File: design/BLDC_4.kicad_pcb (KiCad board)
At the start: 2 copper layers, 80 x 48.9 mm, 101 parts, among them J1 Conn_01x04, P1 PWR_COMM, P2 IN+, P3 IN-, P4 MOTOR3, P5 MOTOR2, P6 MOTOR1, P7 SWD, Q1 Si2302CDS, Q2 Si2302CDS, Q3 Si2302CDS, Q4 Si2302CDS, Q5 Si2302CDS, Q6 Si2302CDS, U1 DRV8302, U2 TC2117, U3 STM32F40X_LQFP64, X1 8MHz 10ppm

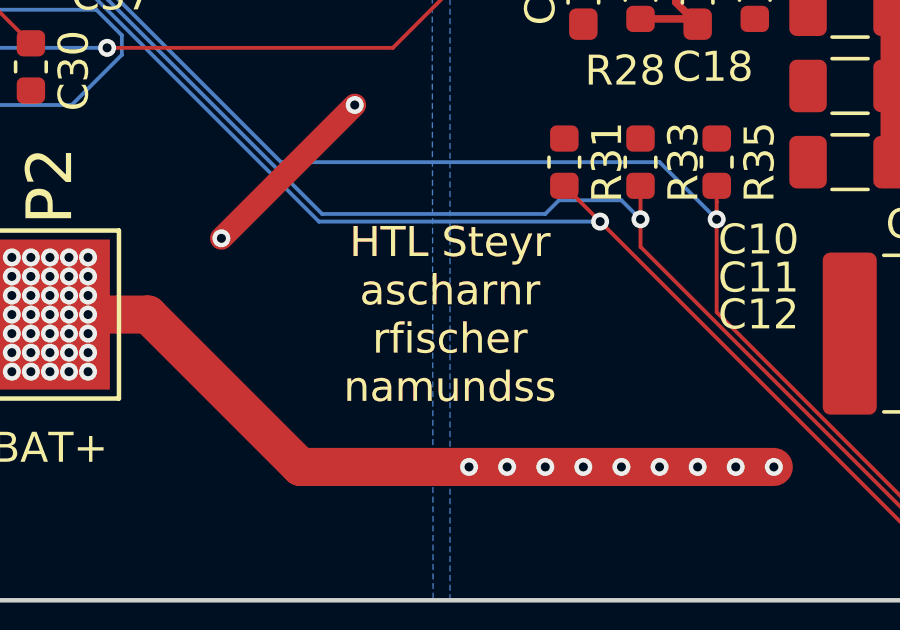
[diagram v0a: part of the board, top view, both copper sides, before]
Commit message: tiny silkscreen change
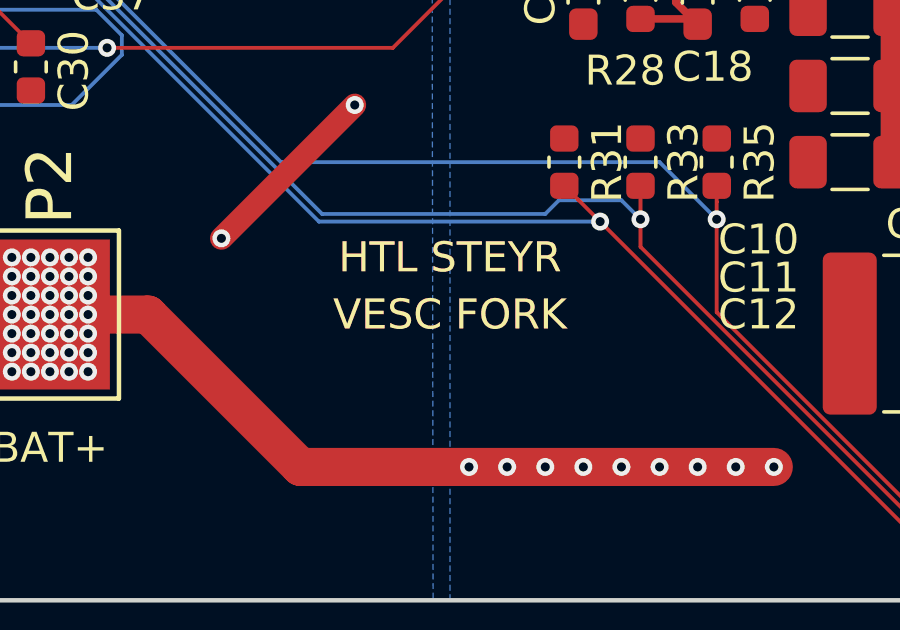
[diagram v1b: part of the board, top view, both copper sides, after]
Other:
- board text added: "HTL STEYR"
- board text added: "VESC FORK"
- board text removed: "HTL Steyr ascharnr rfischer namundss"
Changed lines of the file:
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@@
   (general
     (thickness 1.6)
-    (drawings 12)
+    (drawings 14)
     (tracks 922)
     (zones 0)
@@
     )
   )
+  (gr_text "HTL STEYR" (at 170.815 93.345) (layer F.SilkS)
+    (effects (font (size 1 1) (thickness 0.2)))
+  )
+  (gr_text "VESC FORK\n" (at 170.815 95.25) (layer F.SilkS)
+    (effects (font (size 1 1) (thickness 0.2)))
+  )
+  (gr_text "VESC FORK\n" (at 170.815 95.25) (layer F.Cu)
+    (effects (font (size 1 1) (thickness 0.2)))
+  )
+  (gr_text "HTL STEYR" (at 170.815 93.345) (layer F.Cu)
+    (effects (font (size 1 1) (thickness 0.2)))
+  )
   (gr_line (start 135.255 104.775) (end 210.185 104.775) (layer Edge.Cuts) (width 0.15))
   (gr_line (start 132.715 58.42) (end 132.715 102.235) (layer Edge.Cuts) (width 0.15))
@@
   (gr_arc (start 135.255 102.235) (end 132.715 102.235) (angle -90) (layer Edge.Cuts) (width 0.15))
   (gr_arc (start 135.255 58.42) (end 135.255 55.88) (angle -90) (layer Edge.Cuts) (width 0.15))
-  (gr_text "HTL Steyr\nascharnr\nrfischer\nnamundss" (at 170.815 95.25) (layer F.Cu)
-    (effects (font (size 1 1) (thickness 0.15)))
-  )
-  (gr_text "HTL Steyr\nascharnr\nrfischer\nnamundss" (at 170.815 95.25) (layer F.SilkS)
-    (effects (font (size 1 1) (thickness 0.15)))
-  )
   (gr_text BAT+ (at 157.48 99.695) (layer F.SilkS)
     (effects (font (size 1 1) (thickness 0.15)))

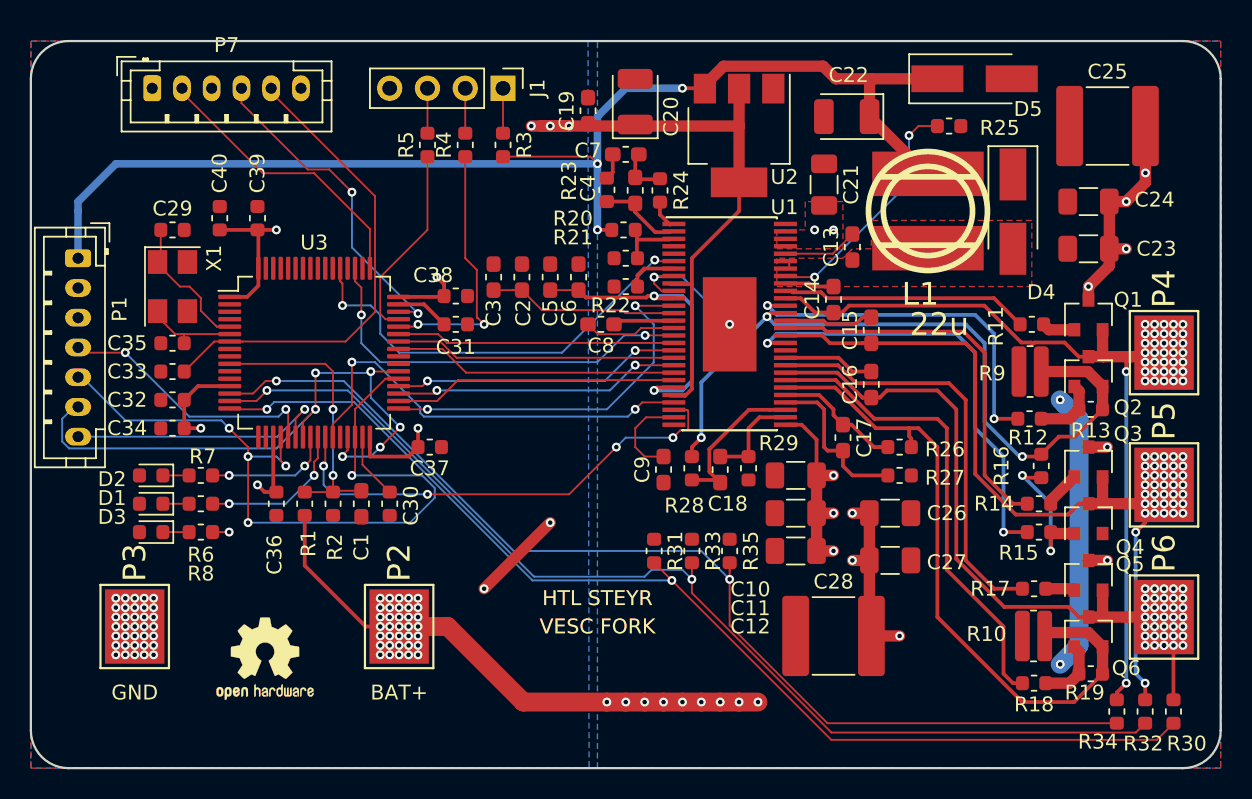
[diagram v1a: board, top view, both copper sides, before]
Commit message: Increasing current carrying capability
Added more vias and dedicated polygons to output stage.
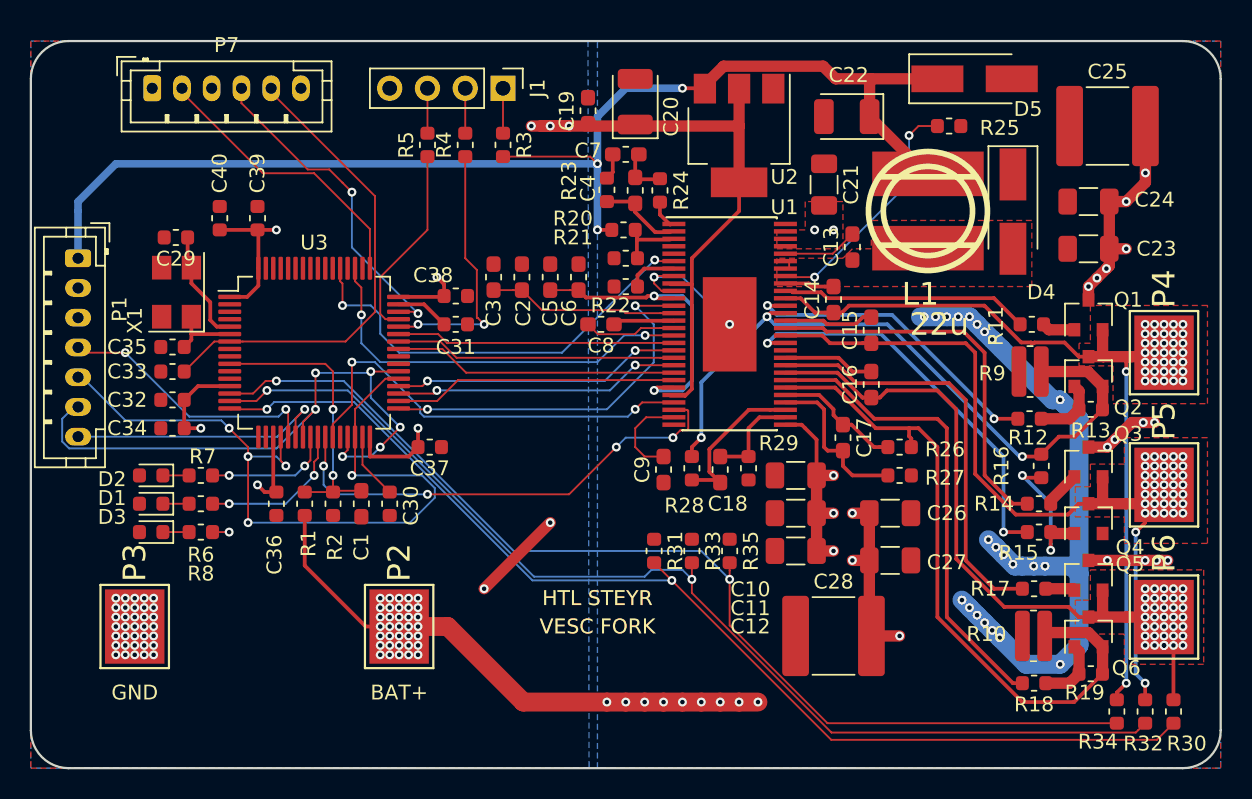
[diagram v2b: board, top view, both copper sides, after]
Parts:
- removed REF**: OSHW-Logo2_7.3x6mm_SilkScreen, Symbol:OSHW-Logo2_7.3x6mm_SilkScreen
- removed REF**: OSHW-Logo2_7.3x6mm_Copper, Symbol:OSHW-Logo2_7.3x6mm_Copper
- moved C29 0.56 mm to (142.5, 69.1), turned to 180 degrees
- moved X1 0.47 mm to (142.5, 72.8), turned to 90 degrees
- moved C35 0.25 mm to (142.2, 76.5)
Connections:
- net /MCU/ADC_TEMP renamed Net-(U3-Pad17)
- X1 pad 1: Net-(C29-Pad1) -> Net-(C35-Pad1)
- X1 pad 2: Net-(C35-Pad1) -> Net-(C29-Pad1)
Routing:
- net GND: track 31.9 -> 59.1 mm, vias 39 -> 59
- net V_SUPPLY: track 86.3 -> 94.2 mm, vias 58 -> 66
- net /Mosfet driver/M_L1: track 24.6 -> 21.3 mm
- net /Mosfet driver/H1_LOW: track 49.8 -> 46.7 mm
- net /Mosfet driver/M_L2: track 30.4 -> 27.5 mm
- net Net-(C29-Pad1): track 9.49 -> 7.68 mm
- net Net-(C35-Pad1): track 6.43 -> 4.81 mm
- added copper zone on F.Cu, net /Mosfet driver/H1_VS
- added copper zone on F.Cu, net /Mosfet driver/H2_VS
- added copper zone on F.Cu, net /Mosfet driver/H3_VS
